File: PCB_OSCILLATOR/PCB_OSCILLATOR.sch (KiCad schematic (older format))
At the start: 70 parts, among them P1 POWER SUPPLY, P2 SPI_AD5270_1, P3 SPI_AD5270_2, P4 SPI_AD9833_1, P5 SPI_AD9833_2, U1 AD5270, U2 AD8421, U3 AD9833, U4 AD5270, U5 AD8421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

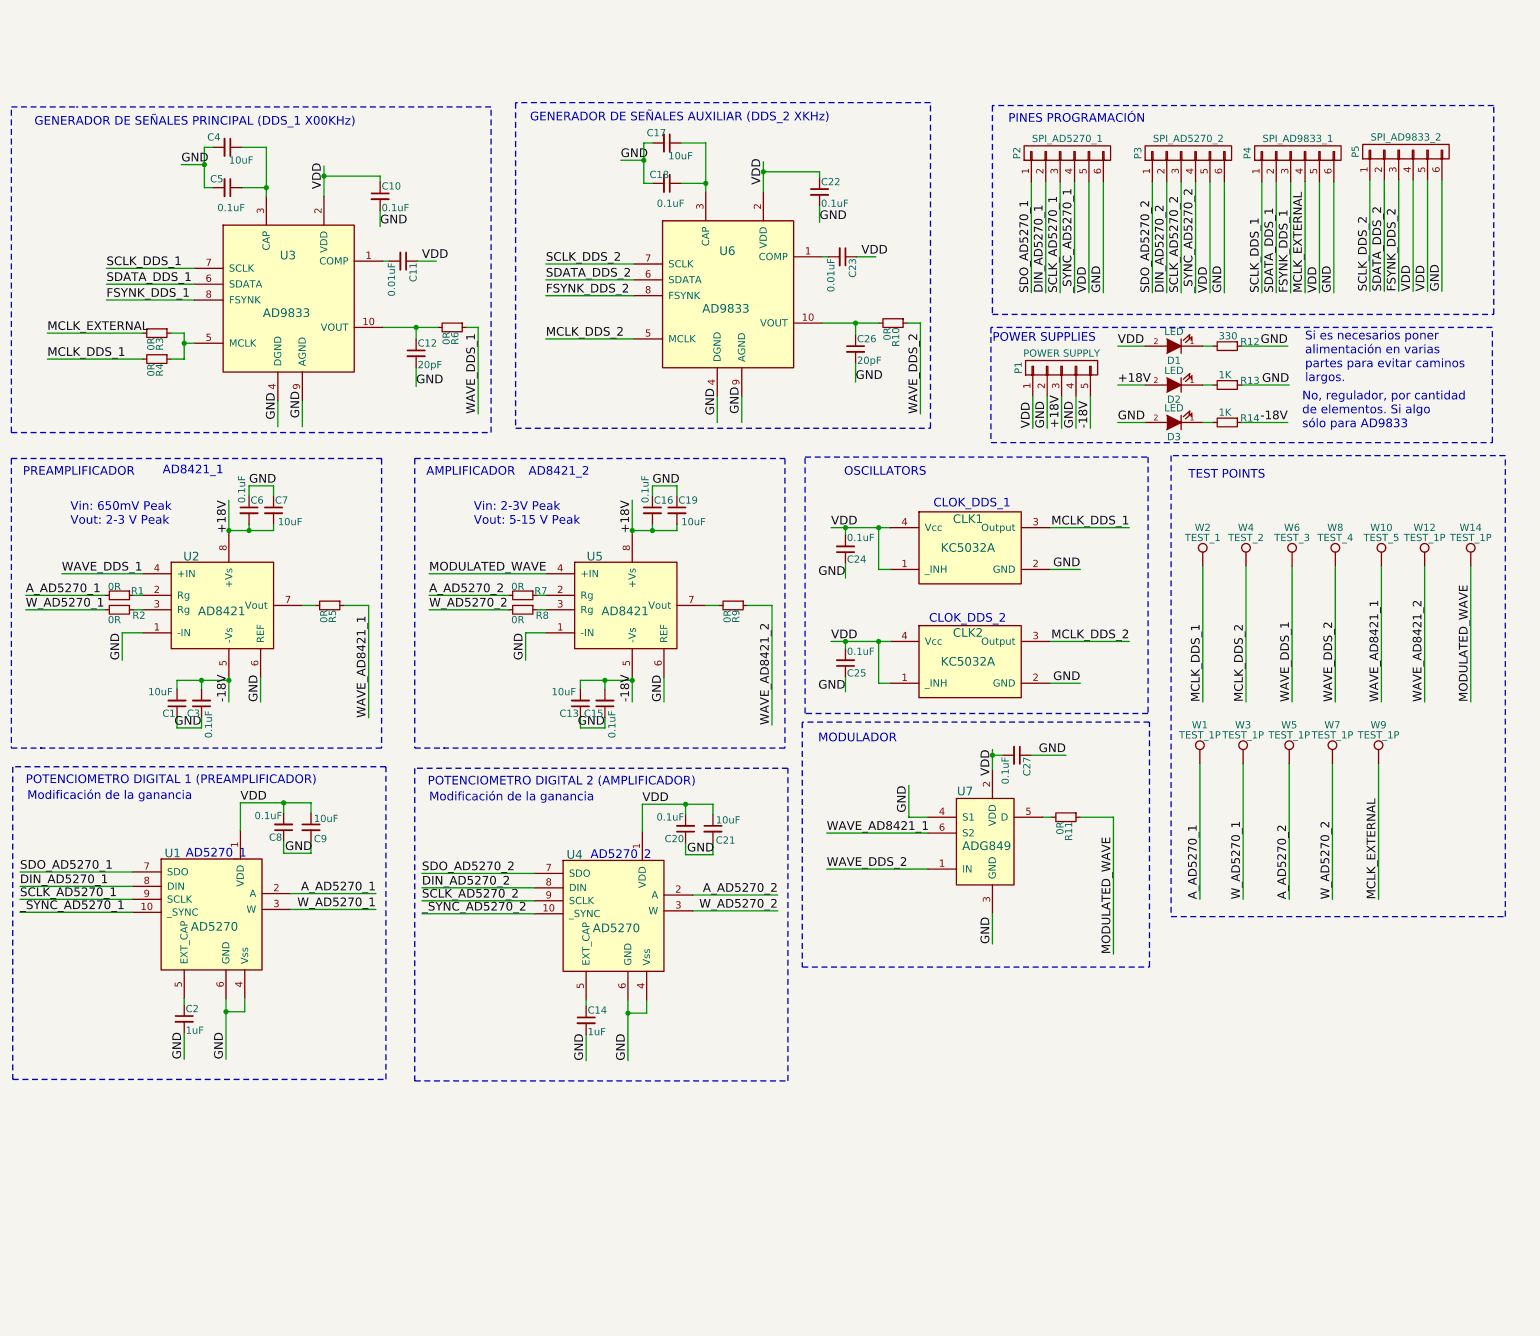
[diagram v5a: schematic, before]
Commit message: Descripción y pruebas BOM
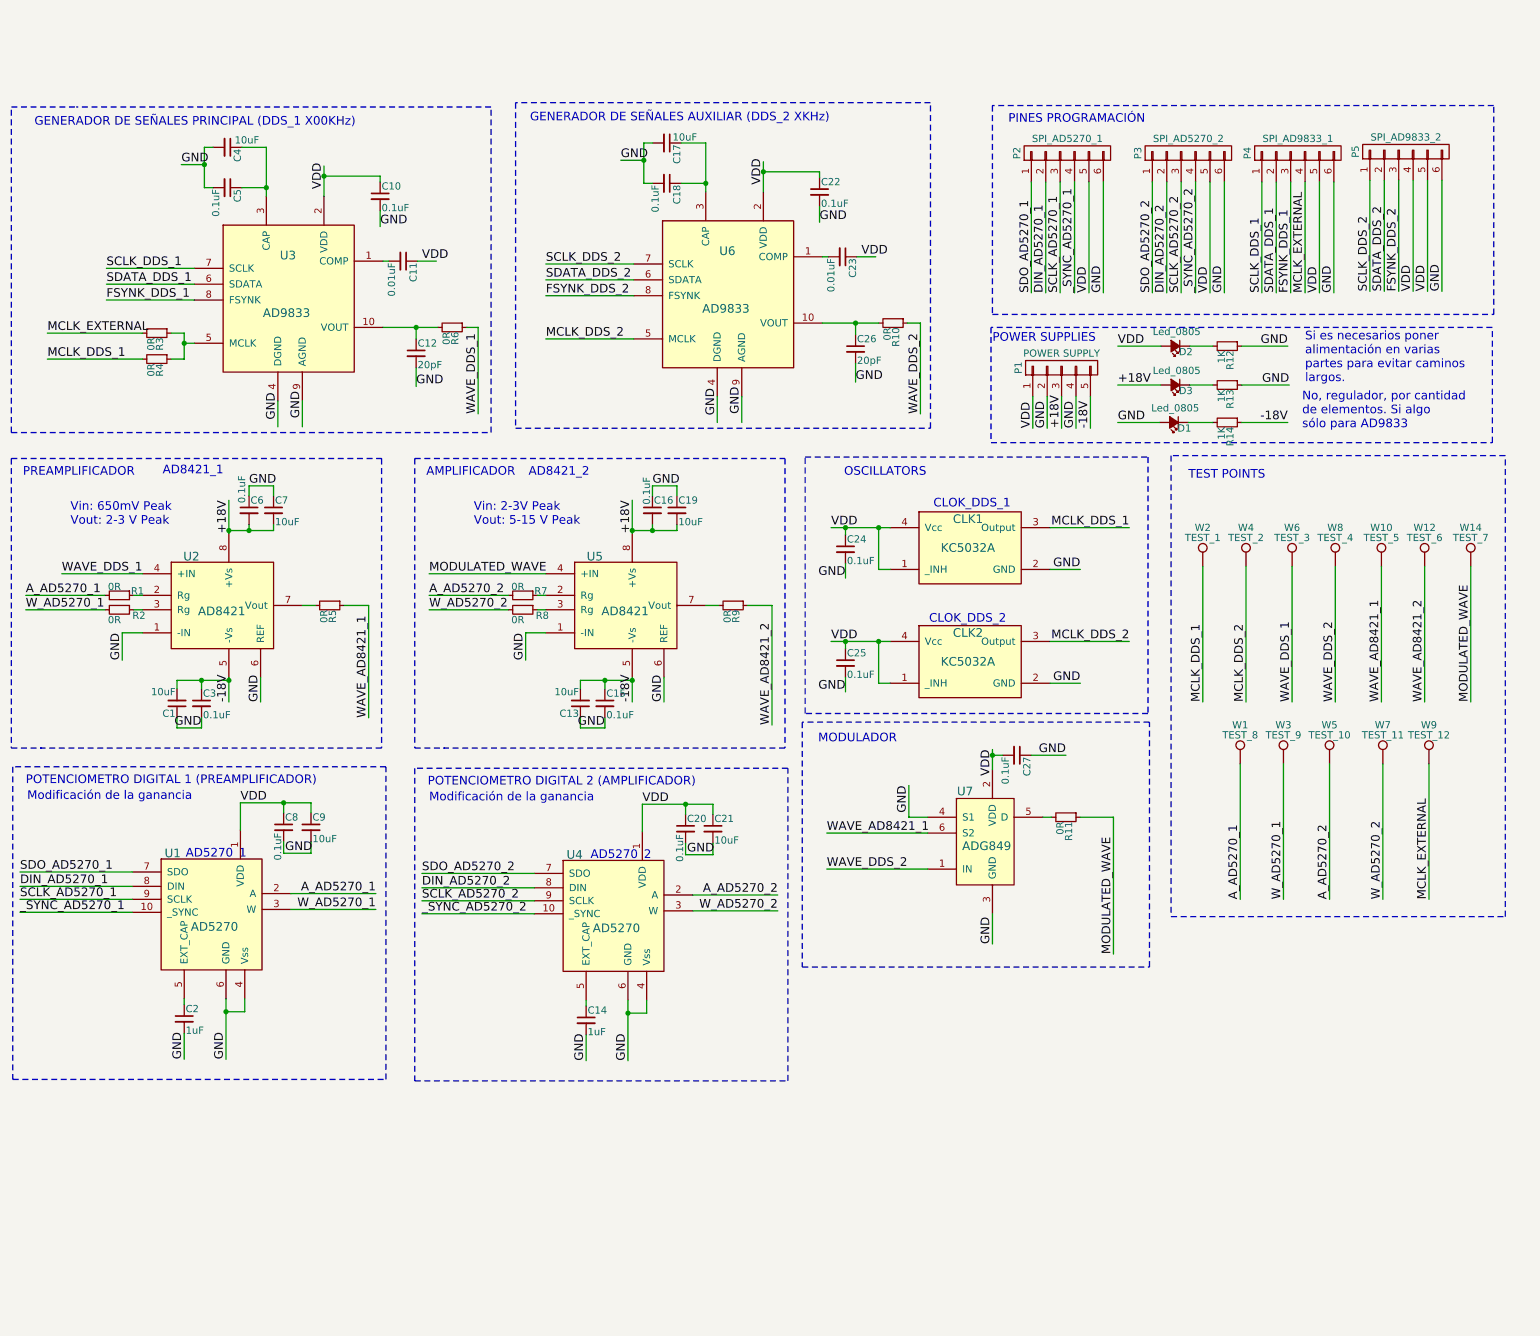
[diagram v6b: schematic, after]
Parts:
- removed C1, C13, C17, C19, C21, C4, C7, C9: 10uF, symbol C_Small
- removed C10, C15, C16, C18, C20, C22, C24, C25, C27, C3, C5, C6, C8: 0.1uF, symbol C_Small
- removed C11, C23: 0.01uF, symbol C_Small
- removed C12, C26: 20pF, symbol C_Small
- removed C14, C2: 1uF, symbol C_Small
- removed D1, D2, D3: LED, symbol LED
- removed R12: 330, symbol R_Small
- removed R13, R14: 1K, symbol R_Small
- added C1, C13, C17, C19, C21, C4, C7, C9: 10uF, Resistors_SMD:R_0805_HandSoldering, symbol 10uF
- added C10, C15, C16, C18, C20, C22, C24, C25, C27, C3, C5, C6, C8: 0.1uF, Resistors_SMD:R_0805_HandSoldering, symbol 0.1uF
- added C11, C23: 0.01uF, Resistors_SMD:R_0805_HandSoldering, symbol 0.01uF
- added C12, C26: 20pF, Resistors_SMD:R_0805_HandSoldering, symbol 20pF
- added C14, C2: 1uF, Resistors_SMD:R_0805_HandSoldering, symbol 1uF
- added D1, D2, D3: Led_0805, Resistors_SMD:R_0805_HandSoldering, symbol Led_0805
- added R12, R13, R14: 1K, Resistors_SMD:R_0805_HandSoldering, symbol 1K
- CLK1, CLK2: footprint (none) -> Foot_Prints_PCB_OSCILLATOR:KC5032A_Foot_Print; OSC XO 25.000MHZ CMOS SMD (none) -> 1253-1043-2-ND
- P1: footprint (none) -> Pin_Headers:Pin_Header_Angled_1x05
- P2, P3, P4, P5: footprint (none) -> Socket_Strips:Socket_Strip_Angled_1x06
- R1, R10, R11, R2, R3, R4, R5, R6, R7, R8, R9: footprint (none) -> Resistors_SMD:R_0805_HandSoldering
- W1: value TEST_1P -> TEST_8; footprint (none) -> Measurement_Points:Measurement_Point_Round-TH_Small
- W10, W2, W4, W6, W8: footprint (none) -> Measurement_Points:Measurement_Point_Round-TH_Small
- W12: value TEST_1P -> TEST_6; footprint (none) -> Measurement_Points:Measurement_Point_Round-TH_Small
- W14: value TEST_1P -> TEST_7; footprint (none) -> Measurement_Points:Measurement_Point_Round-TH_Small
- W3: value TEST_1P -> TEST_9; footprint (none) -> Measurement_Points:Measurement_Point_Round-TH_Small
- W5: value TEST_1P -> TEST_10; footprint (none) -> Measurement_Points:Measurement_Point_Round-TH_Small
- W7: value TEST_1P -> TEST_11; footprint (none) -> Measurement_Points:Measurement_Point_Round-TH_Small
- W9: value TEST_1P -> TEST_12; footprint (none) -> Measurement_Points:Measurement_Point_Round-TH_Small
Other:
- moved on the sheet: W1, W3, W5, W7, W9

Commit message: Faltan Cambios Menores
Voy a hacer simulaciones con el ADG819 y diagrama de bloques para
corregir errores y verificar si hacen falta poner algunos test points.
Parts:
- removed U7: ADG849, symbol ADG849
- added C28: 0.1uF, Resistors_SMD:R_0805_HandSoldering, symbol 0.1uF
- added C29: 10uF, Resistors_SMD:R_0805_HandSoldering, symbol 10uF
- added U7: ADG819, Housings_SSOP:MSOP-8_3x3mm_Pitch0.65mm, symbol ADG819
- U1, U3, U4, U6: footprint (none) -> Housings_SSOP:MSOP-10-1EP_3x3mm_Pitch0.5mm
- U2, U5: footprint (none) -> Housings_SOIC:SOIC-8_3.9x4.9mm_Pitch1.27mm
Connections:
- wire segments 214 -> 211
- no-connect marks 0 -> 11
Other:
- note added: "Capacitores\nDesacople en\nentrada\n"
- note added: "FALTA CAMBIAR LOS CAP DE 10uF POR POLARIZADOS"
- note added: "Regletas de 6 pines, por si \nnecesito mas entradas para VDD"
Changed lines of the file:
@@
 F 0 "U3" H 2600 2270 60  0000 C CNN
 F 1 "AD9833" H 2590 1870 60  0000 C CNN
-F 2 "" H 2420 2030 60  0001 C CNN
+F 2 "Housings_SSOP:MSOP-10-1EP_3x3mm_Pitch0.5mm" H 2420 2030 60  0001 C CNN
 F 3 "" H 2420 2030 60  0000 C CNN
 	1    2620 2000
@@
 F 0 "U6" H 5650 2240 60  0000 C CNN
 F 1 "AD9833" H 5640 1840 60  0000 C CNN
-F 2 "" H 5470 2000 60  0001 C CNN
+F 2 "Housings_SSOP:MSOP-10-1EP_3x3mm_Pitch0.5mm" H 5470 2000 60  0001 C CNN
 F 3 "" H 5470 2000 60  0000 C CNN
 	1    5670 1970
@@
 F 0 "U2" H 1930 4440 60  0000 C CNN
 F 1 "AD8421" H 2140 4060 60  0000 C CNN
-F 2 "" H 1980 3830 60  0001 C CNN
+F 2 "Housings_SOIC:SOIC-8_3.9x4.9mm_Pitch1.27mm" H 1980 3830 60  0001 C CNN
 F 3 "" H 1980 3830 60  0000 C CNN
 	1    2150 4130
@@
 F 0 "U5" H 4730 4440 60  0000 C CNN
 F 1 "AD8421" H 4940 4060 60  0000 C CNN
-F 2 "" H 4780 3830 60  0001 C CNN
+F 2 "Housings_SOIC:SOIC-8_3.9x4.9mm_Pitch1.27mm" H 4780 3830 60  0001 C CNN
 F 3 "" H 4780 3830 60  0000 C CNN
 	1    4950 4130
@@
 W_AD5270_2
 $Comp
-L ADG849 U7
-U 1 1 590F8A79
-P 7440 5830
-F 0 "U7" H 7300 6210 60  0000 C CNN
-F 1 "ADG849" H 7450 5830 60  0000 C CNN
-F 2 "" H 7440 5830 60  0001 C CNN
-F 3 "" H 7440 5830 60  0000 C CNN
-	1    7440 5830
-	1    0    0    -1
-$EndComp
-$Comp
 L R_Small R11
 U 1 1 590FBD26
@@
 F 0 "U1" H 1800 6460 60  0000 C CNN
 F 1 "AD5270" H 2090 5950 60  0000 C CNN
-F 2 "" H 2190 6080 60  0001 C CNN
+F 2 "Housings_SSOP:MSOP-10-1EP_3x3mm_Pitch0.5mm" H 2190 6080 60  0001 C CNN
 F 3 "" H 2190 6080 60  0000 C CNN
 	1    1560 6170
@@
 F 0 "U4" H 4590 6470 60  0000 C CNN
 F 1 "AD5270" H 4880 5960 60  0000 C CNN
-F 2 "" H 4980 6090 60  0001 C CNN
+F 2 "Housings_SSOP:MSOP-10-1EP_3x3mm_Pitch0.5mm" H 4980 6090 60  0001 C CNN
 F 3 "" H 4980 6090 60  0000 C CNN
 	1    4350 6180
@@
 Text Label 8060 1990 1    60   ~ 0
 _SYNC_AD5270_1
-Text Label 8160 1990 1    60   ~ 0
-VDD
-Text Label 8260 1990 1    60   ~ 0
-GND
 $Comp
 L CONN_01X06 P3
@@
 Text Label 8900 1990 1    60   ~ 0
 _SYNC_AD5270_2
-Text Label 9000 1990 1    60   ~ 0
-VDD
-Text Label 9100 1990 1    60   ~ 0
-GND
 $Comp
 L CONN_01X06 P4
@@
 Text Label 9560 1990 1    60   ~ 0
 FSYNK_DDS_1
-Text Label 9760 1990 1    60   ~ 0
-VDD
-Text Label 9860 1990 1    60   ~ 0
-GND
 $Comp
 L CONN_01X06 P5
@@
 Text Label 10310 1980 1    60   ~ 0
 FSYNK_DDS_2
-Text Label 10510 1980 1    60   ~ 0
-VDD
-Text Label 10610 1980 1    60   ~ 0
-GND
 Text Label 9660 1990 1    60   ~ 0
 MCLK_EXTERNAL
-Text Label 10410 1980 1    60   ~ 0
-VDD
 Text Notes 7600 820  0    60   ~ 0
 PINES PROGRAMACIÓN
@@
 	8060 1220 8060 1990
 Wire Wire Line
-	8160 1220 8160 1990
-Wire Wire Line
-	8260 1220 8260 1990
-Wire Wire Line
 	8600 1220 8600 1990
 Wire Wire Line
@@
 	8900 1220 8900 1990
 Wire Wire Line
-	9000 1220 9000 1990
-Wire Wire Line
-	9100 1220 9100 1990
-Wire Wire Line
 	9360 1220 9360 1990
 Wire Wire Line
@@
 	9660 1220 9660 1990
 Wire Wire Line
-	9760 1220 9760 1990
-Wire Wire Line
-	9860 1220 9860 1990
-Wire Wire Line
 	10110 1210 10110 1980
 Wire Wire Line
@@
 Wire Wire Line
 	10310 1210 10310 1980
-Wire Wire Line
-	10410 1210 10410 1980
-Wire Wire Line
-	10510 1210 10510 1980
-Wire Wire Line
-	10610 1210 10610 1980
 Wire Notes Line
 	7490 690  7490 2140
@@
 	1    0    0    -1
 $EndComp
+$Comp
+L ADG819 U7
+U 1 1 5911630B
+P 7440 5830
+F 0 "U7" H 7300 6210 60  0000 C CNN
+F 1 "ADG819" H 7450 5830 60  0000 C CNN
+F 2 "Housings_SSOP:MSOP-8_3x3mm_Pitch0.65mm" H 7200 6110 60  0001 C CNN
+F 3 "" H 7440 5830 60  0000 C CNN
+	1    7440 5830
+	1    0    0    -1
+$EndComp
+NoConn ~ 7840 5760
+NoConn ~ 7840 5870
+NoConn ~ 8160 1220
+NoConn ~ 8260 1220
+NoConn ~ 9000 1220
+NoConn ~ 9100 1220
+NoConn ~ 9760 1220
+NoConn ~ 9860 1220
+NoConn ~ 10410 1210
+NoConn ~ 10510 1210
+NoConn ~ 10610 1210
+Text Notes 9040 870  0    60   ~ 0
+Regletas de 6 pines, por si \nnecesito mas entradas para VDD
+$Comp
+L 0.1uF C28
+U 1 1 5912437D
+P 6360 7370
+F 0 "C28" H 6370 7440 50  0000 L CNN
+F 1 "0.1uF" H 6370 7290 50  0000 L CNN
+F 2 "Resistors_SMD:R_0805_HandSoldering" H 6270 7340 50  0001 C CNN
+F 3 "" H 6370 7440 50  0001 C CNN
+F 4 "478-1395-2-ND" H 6470 7540 60  0001 C CNN "Digi-Key Part Number"
+	1    6360 7370
+	1    0    0    -1
+$EndComp
+$Comp
+L 10uF C29
+U 1 1 59124E81
+P 6650 7370
+F 0 "C29" H 6660 7440 50  0000 L CNN
+F 1 "10uF" H 6660 7290 50  0000 L CNN
+F 2 "Resistors_SMD:R_0805_HandSoldering" H 6560 7340 50  0001 C CNN
+F 3 "" H 6660 7440 50  0001 C CNN
+F 4 "490-5523-2-ND" H 6760 7540 60  0001 C CNN "25V"
+	1    6650 7370
+	1    0    0    -1
+$EndComp
+Text Notes 1630 370  0    200  ~ 40
+FALTA CAMBIAR LOS CAP DE 10uF POR POLARIZADOS
+Wire Wire Line
+	6360 7270 6360 7100
+Wire Wire Line
+	6360 7100 6650 7100
+Wire Wire Line
+	6650 7100 6650 7270
+Wire Wire Line
+	6650 7470 6650 7630
+Wire Wire Line
+	6650 7630 6360 7630
+Wire Wire Line
+	6360 7630 6360 7470
+Text Label 6610 7630 2    60   ~ 0
+GND
+Text Label 6430 7100 0    60   ~ 0
+VDD
+Wire Notes Line
+	6130 6710 6130 7730
+Wire Notes Line
+	6130 7730 6920 7730
+Wire Notes Line
+	6920 7730 6920 6710
+Wire Notes Line
+	6920 6710 6130 6710
+Text Notes 6150 6980 0    60   ~ 0
+Capacitores\nDesacople en\nentrada\n
 $EndSCHEMATC

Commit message: Adjunto Diagrama de bloques
Está en carpeta principal con el nombre de las señales.
Falta Validar funcionamiento del ADG819 y agregar puntos para pruebas
(pines, sin contar los test points)
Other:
- note added: "(Digital Potentiometer)"
- note added: "GAIN VARIABLE\nAMPLIFIER_1"
- note added: "GAIN VARIABLE\nAMPLIFIER_2"
- note added: "GAIN_CONTROL_1"
- note added: "GAIN_CONTROL_2"
- note added: "GENERATOR SIGNAL (DDS_1 X00KHz)\n"
- note added: "GENERATOR SIGNAL (DDS_2 XKHz)\n"
- note added: "MULTIPLEXER"
- note added: "Vin: 3V Peak (Max)\nVout: 15 V Peak (Max)"
- note added: "Vin: 650mV Peak (Max)\nVout: 3 V Peak (Max)"
- note removed: "AMPLIFICADOR"
- note removed: "GENERADOR DE SEÑALES AUXILIAR (DDS_2 XKHz)\n"
- note removed: "GENERADOR DE SEÑALES PRINCIPAL (DDS_1 X00KHz)\n"
- note removed: "MODULADOR"
- note removed: "Modificación de la ganancia"
- note removed: "POTENCIOMETRO DIGITAL 1 (PREAMPLIFICADOR)"
- note removed: "POTENCIOMETRO DIGITAL 2 (AMPLIFICADOR)"
- note removed: "PREAMPLIFICADOR"
- note removed: "Vin: 2-3V Peak\nVout: 5-15 V Peak"
- note removed: "Vin: 650mV Peak\nVout: 2-3 V Peak"
- moved on the sheet: W1, W10, W12, W14, W2, W3, W4, W5, W6, W7, W8, W9
